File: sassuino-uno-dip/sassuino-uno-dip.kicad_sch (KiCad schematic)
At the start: 30 parts, among them J1 USB_B, J10 OSCPWR_HDR, J2 POWER2_HDR, J3 ICSP_HDR, J4 POWER_HDR, J5 PORTC_HDR, J6 PORTB_HDR, J7 PORTD_HDR, J8 XTAL2_HDR, J9 XTAL1_HDR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

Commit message: Add the actual footprint/model of the pushbutton switch I'm using.
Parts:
- removed SW1: RESET_SW, Button_Switch_THT:SW_PUSH_6mm, symbol Switch:SW_Push
- added SW1: RESET_SW, 0SassuinoFP:SW4_1825910-B_TEC, symbol Switch:SW_Push_Dual
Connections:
- net GND: now also SW1.1, SW1.3
- net ~{RESET}: now also SW1.2, SW1.4
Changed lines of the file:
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@@
   (junction (at 209.55 64.77) (diameter 0) (color 0 0 0 0)
+  )
+  (junction (at 113.03 74.93) (diameter 0) (color 0 0 0 0)
+  )
+  (junction (at 113.03 64.77) (diameter 0) (color 0 0 0 0)
   )
   (junction (at 172.72 38.1) (diameter 0) (color 0 0 0 0)
@@
     (stroke (width 0) (type default) (color 0 0 0 0))
   )
+  (wire (pts (xy 113.03 74.93) (xy 115.57 74.93))
+    (stroke (width 0) (type default) (color 0 0 0 0))
+  )
   (wire (pts (xy 25.4 148.59) (xy 39.37 148.59))
     (stroke (width 0) (type default) (color 0 0 0 0))
@@
     (stroke (width 0) (type default) (color 0 0 0 0))
   )
+  (wire (pts (xy 110.49 64.77) (xy 113.03 64.77))
+    (stroke (width 0) (type default) (color 0 0 0 0))
+  )
   (wire (pts (xy 210.82 100.33) (xy 195.58 100.33))
     (stroke (width 0) (type default) (color 0 0 0 0))
@@
     (stroke (width 0) (type default) (color 0 0 0 0))
   )
+  (wire (pts (xy 110.49 74.93) (xy 113.03 74.93))
+    (stroke (width 0) (type default) (color 0 0 0 0))
+  )
   (wire (pts (xy 58.42 55.88) (xy 60.96 55.88))
     (stroke (width 0) (type default) (color 0 0 0 0))
@@
     (stroke (width 0) (type default) (color 0 0 0 0))
   )
+  (wire (pts (xy 113.03 76.2) (xy 113.03 74.93))
+    (stroke (width 0) (type default) (color 0 0 0 0))
+  )
   (wire (pts (xy 209.55 64.77) (xy 210.82 64.77))
     (stroke (width 0) (type default) (color 0 0 0 0))
@@
     (stroke (width 0) (type default) (color 0 0 0 0))
   )
+  (wire (pts (xy 113.03 64.77) (xy 115.57 64.77))
+    (stroke (width 0) (type default) (color 0 0 0 0))
+  )
   (wire (pts (xy 34.29 153.67) (xy 34.29 156.21))
     (stroke (width 0) (type default) (color 0 0 0 0))
@@
   )
   (wire (pts (xy 58.42 53.34) (xy 60.96 53.34))
+    (stroke (width 0) (type default) (color 0 0 0 0))
+  )
+  (wire (pts (xy 113.03 60.96) (xy 113.03 64.77))
     (stroke (width 0) (type default) (color 0 0 0 0))
   )
@@
     )
     (pin "1")
+  )
+  (symbol (lib_id "Switch:SW_Push_Dual") (at 110.49 69.85 90) (unit 1)
+    (in_bom yes) (on_board yes) (fields_autoplaced)
+    (property "Reference" "SW1" (id 0) (at 116.84 68.5799 90)
+      (effects (font (size 1.27 1.27)) (justify right))
+    )
+    (property "Value" "RESET_SW" (id 1) (at 116.84 71.1199 90)
+      (effects (font (size 1.27 1.27)) (justify right))
+    )
+    (property "Footprint" "0SassuinoFP:SW4_1825910-B_TEC" (id 2) (at 105.41 69.85 0)
+      (effects (font (size 1.27 1.27)) hide)
+    )
+    (property "Datasheet" "https://www.te.com/usa-en/product-1825910-7.datasheet.pdf" (id 3) (at 105.41 69.85 0)
+      (effects (font (size 1.27 1.27)) hide)
+    )
+    (pin "1")
+    (pin "2")
+    (pin "3")
+    (pin "4")
   )
   (symbol (lib_id "Connector_Generic:Conn_01x08") (at 44.45 148.59 0) (unit 1)
@@
     (pin "2")
   )
-  (symbol (lib_id "Switch:SW_Push") (at 113.03 66.04 90) (unit 1)
-    (in_bom yes) (on_board yes) (fields_autoplaced)
-    (property "Reference" "SW1" (id 0) (at 114.3 64.7699 90)
-      (effects (font (size 1.27 1.27)) (justify right))
-    )
-    (property "Value" "RESET_SW" (id 1) (at 114.3 67.3099 90)
-      (effects (font (size 1.27 1.27)) (justify right))
-    )
-    (property "Footprint" "Button_Switch_THT:SW_PUSH_6mm" (id 2) (at 107.95 66.04 0)
-      (effects (font (size 1.27 1.27)) hide)
-    )
-    (property "Datasheet" "~" (id 3) (at 107.95 66.04 0)
-      (effects (font (size 1.27 1.27)) hide)
-    )
-    (pin "1")
-    (pin "2")
-  )
   (symbol (lib_id "power:VCC") (at 102.87 182.88 0) (unit 1)
     (in_bom yes) (on_board yes) (fields_autoplaced)
@@
     (pin "1")
   )
-  (symbol (lib_id "power:GND") (at 113.03 71.12 0) (unit 1)
-    (in_bom yes) (on_board yes) (fields_autoplaced)
-    (property "Reference" "#PWR0111" (id 0) (at 113.03 77.47 0)
-      (effects (font (size 1.27 1.27)) hide)
-    )
-    (property "Value" "GND" (id 1) (at 113.03 76.2 0))
-    (property "Footprint" "" (id 2) (at 113.03 71.12 0)
-      (effects (font (size 1.27 1.27)) hide)
-    )
-    (property "Datasheet" "" (id 3) (at 113.03 71.12 0)
+  (symbol (lib_id "power:GND") (at 113.03 76.2 0) (unit 1)
+    (in_bom yes) (on_board yes) (fields_autoplaced)
+    (property "Reference" "#PWR0111" (id 0) (at 113.03 82.55 0)
+      (effects (font (size 1.27 1.27)) hide)
+    )
+    (property "Value" "GND" (id 1) (at 113.03 81.28 0))
+    (property "Footprint" "" (id 2) (at 113.03 76.2 0)
+      (effects (font (size 1.27 1.27)) hide)
+    )
+    (property "Datasheet" "" (id 3) (at 113.03 76.2 0)
       (effects (font (size 1.27 1.27)) hide)
     )
@@
       (reference "R3") (unit 1) (value "10K") (footprint "Resistor_SMD:R_1206_3216Metric")
     )
-    (path "/75a043c9-9e49-4414-80bf-ac27bb36e4e0"
-      (reference "SW1") (unit 1) (value "RESET_SW") (footprint "Button_Switch_THT:SW_PUSH_6mm")
+    (path "/126610dc-fcb3-4c6a-b444-35d67e624073"
+      (reference "SW1") (unit 1) (value "RESET_SW") (footprint "0SassuinoFP:SW4_1825910-B_TEC")
     )
     (path "/d4ca7310-101e-466b-b5be-c8ae191213f7"

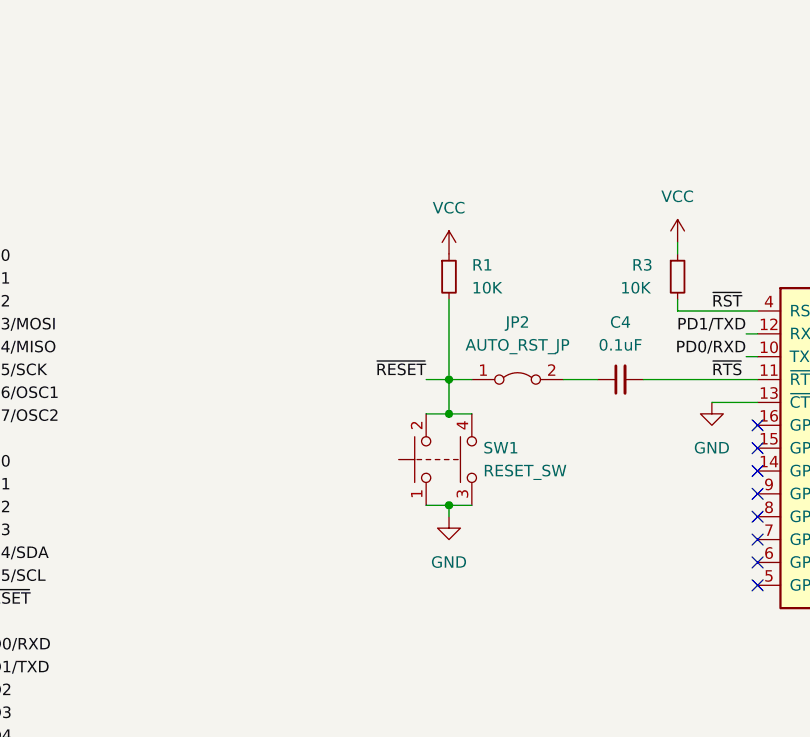
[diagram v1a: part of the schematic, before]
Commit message: Add a clamp diode to the reset circuit.
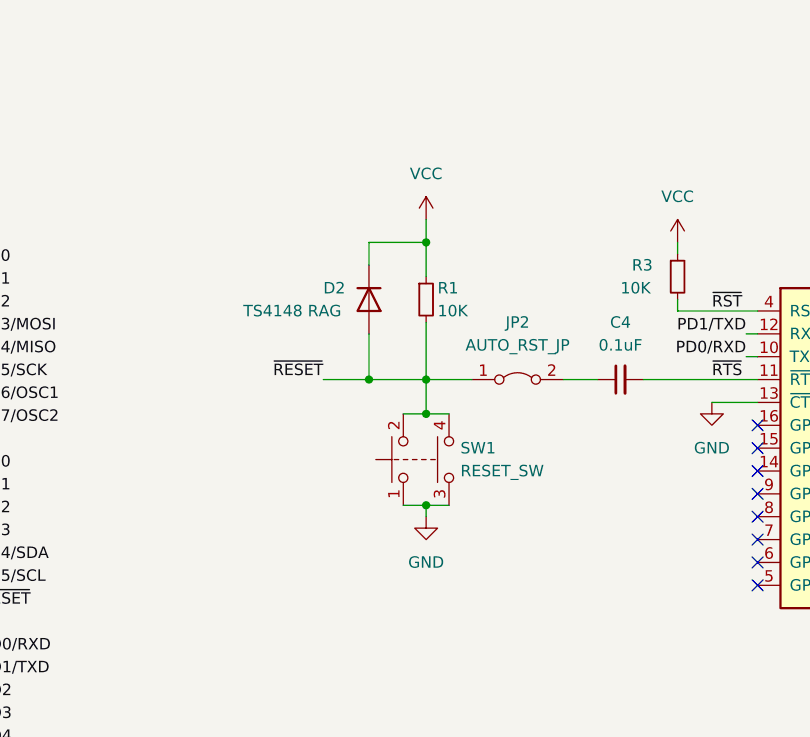
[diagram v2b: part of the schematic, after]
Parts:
- added D2: TS4148 RAG, Diode_SMD:D_1206_3216Metric, symbol Device:D
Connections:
- net VCC: now also D2.1 (K)
- net ~{RESET}: now also D2.2 (A)
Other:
- moved on the sheet: R1, SW1

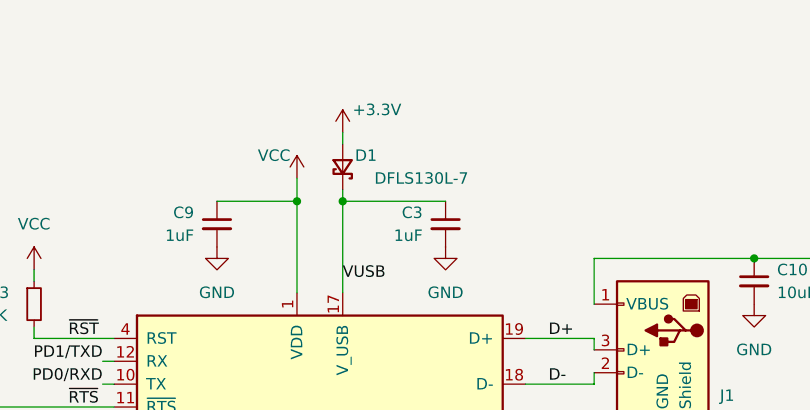
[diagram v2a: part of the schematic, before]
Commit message: Add missing PWR_FLAG so the schematic passes the ERC again.
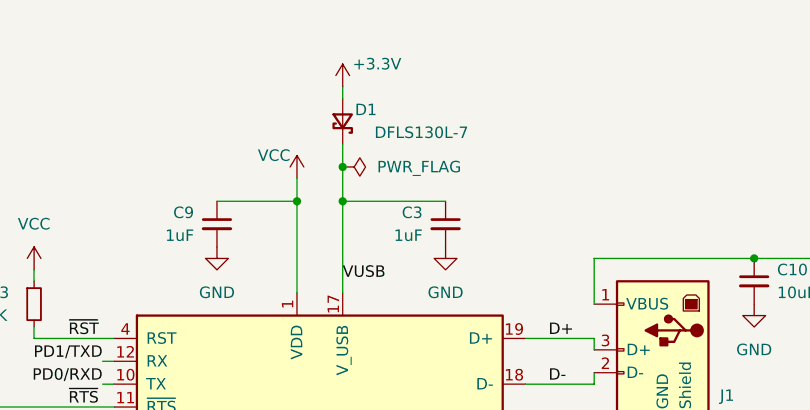
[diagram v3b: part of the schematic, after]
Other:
- moved on the sheet: D1
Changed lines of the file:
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@@
   (junction (at 204.47 138.43) (diameter 0) (color 0 0 0 0)
+  )
+  (junction (at 172.72 34.29) (diameter 0) (color 0 0 0 0)
   )
   (junction (at 110.49 45.72) (diameter 0) (color 0 0 0 0)
@@
     (stroke (width 0) (type default) (color 0 0 0 0))
   )
-  (wire (pts (xy 172.72 36.83) (xy 172.72 38.1))
+  (wire (pts (xy 172.72 31.75) (xy 172.72 34.29))
     (stroke (width 0) (type default) (color 0 0 0 0))
   )
@@
     (stroke (width 0) (type default) (color 0 0 0 0))
   )
-  (wire (pts (xy 172.72 30.48) (xy 172.72 31.75))
+  (wire (pts (xy 172.72 25.4) (xy 172.72 26.67))
     (stroke (width 0) (type default) (color 0 0 0 0))
   )
@@
   )
   (wire (pts (xy 193.04 53.34) (xy 200.66 53.34))
+    (stroke (width 0) (type default) (color 0 0 0 0))
+  )
+  (wire (pts (xy 172.72 34.29) (xy 172.72 38.1))
     (stroke (width 0) (type default) (color 0 0 0 0))
   )
@@
     (pin "1")
   )
+  (symbol (lib_id "power:PWR_FLAG") (at 172.72 34.29 270) (unit 1)
+    (in_bom yes) (on_board yes) (fields_autoplaced)
+    (property "Reference" "#FLG0101" (id 0) (at 174.625 34.29 0)
+      (effects (font (size 1.27 1.27)) hide)
+    )
+    (property "Value" "PWR_FLAG" (id 1) (at 176.53 34.2899 90)
+      (effects (font (size 1.27 1.27)) (justify left))
+    )
+    (property "Footprint" "" (id 2) (at 172.72 34.29 0)
+      (effects (font (size 1.27 1.27)) hide)
+    )
+    (property "Datasheet" "~" (id 3) (at 172.72 34.29 0)
+      (effects (font (size 1.27 1.27)) hide)
+    )
+    (pin "1")
+  )
   (symbol (lib_id "power:VCC") (at 234.95 146.05 0) (unit 1)
     (in_bom yes) (on_board yes) (fields_autoplaced)
@@
     (pin "2")
   )
-  (symbol (lib_id "Device:D_Schottky_Small") (at 172.72 34.29 270) (mirror x) (unit 1)
+  (symbol (lib_id "Device:D_Schottky_Small") (at 172.72 29.21 270) (mirror x) (unit 1)
     (in_bom yes) (on_board yes)
-    (property "Reference" "D1" (id 0) (at 176.53 33.02 90)
+    (property "Reference" "D1" (id 0) (at 176.53 27.94 90)
       (effects (font (size 1.27 1.27)) (justify right))
     )
-    (property "Value" "DFLS130L-7" (id 1) (at 186.69 35.56 90)
+    (property "Value" "DFLS130L-7" (id 1) (at 186.69 30.48 90)
       (effects (font (size 1.27 1.27)) (justify right))
     )
-    (property "Footprint" "Diode_SMD:D_PowerDI-123" (id 2) (at 172.72 34.29 90)
-      (effects (font (size 1.27 1.27)) hide)
-    )
-    (property "Datasheet" "https://www.diodes.com/assets/Datasheets/DFLS130L.pdf" (id 3) (at 172.72 34.29 90)
+    (property "Footprint" "Diode_SMD:D_PowerDI-123" (id 2) (at 172.72 29.21 90)
+      (effects (font (size 1.27 1.27)) hide)
+    )
+    (property "Datasheet" "https://www.diodes.com/assets/Datasheets/DFLS130L.pdf" (id 3) (at 172.72 29.21 90)
       (effects (font (size 1.27 1.27)) hide)
     )
@@
     (pin "1")
   )
-  (symbol (lib_id "power:+3.3V") (at 172.72 30.48 0) (mirror y) (unit 1)
+  (symbol (lib_id "power:+3.3V") (at 172.72 25.4 0) (mirror y) (unit 1)
     (in_bom yes) (on_board yes)
-    (property "Reference" "#PWR02" (id 0) (at 172.72 34.29 0)
-      (effects (font (size 1.27 1.27)) hide)
-    )
-    (property "Value" "+3.3V" (id 1) (at 176.53 27.94 0))
-    (property "Footprint" "" (id 2) (at 172.72 30.48 0)
-      (effects (font (size 1.27 1.27)) hide)
-    )
-    (property "Datasheet" "" (id 3) (at 172.72 30.48 0)
+    (property "Reference" "#PWR02" (id 0) (at 172.72 29.21 0)
+      (effects (font (size 1.27 1.27)) hide)
+    )
+    (property "Value" "+3.3V" (id 1) (at 176.53 22.86 0))
+    (property "Footprint" "" (id 2) (at 172.72 25.4 0)
+      (effects (font (size 1.27 1.27)) hide)
+    )
+    (property "Datasheet" "" (id 3) (at 172.72 25.4 0)
       (effects (font (size 1.27 1.27)) hide)
     )
@@
   )
   (symbol_instances
+    (path "/5363497a-4179-4df5-acfd-489da65e4609"
+      (reference "#FLG0101") (unit 1) (value "PWR_FLAG") (footprint "")
+    )
     (path "/1eb342cb-074c-4750-9652-926960d0a3e3"
       (reference "#FLG0102") (unit 1) (value "PWR_FLAG") (footprint "")

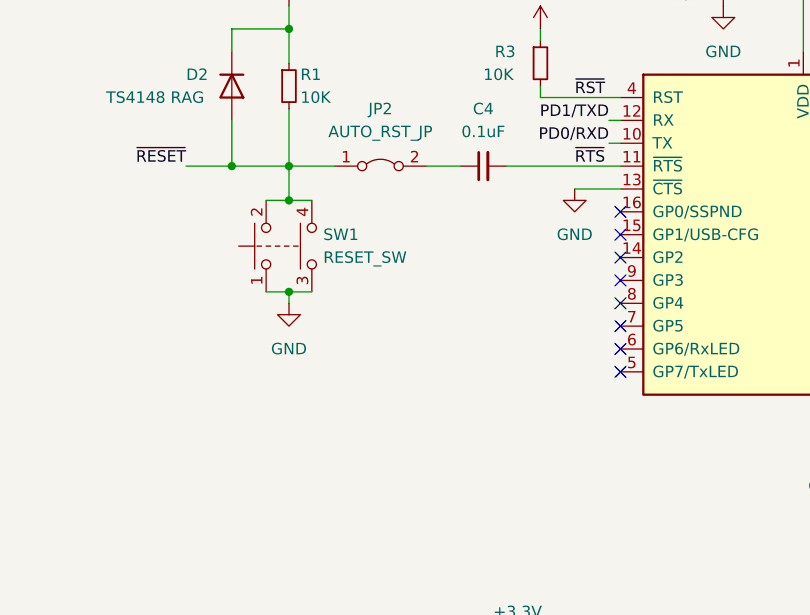
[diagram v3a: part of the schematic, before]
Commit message: Improve the reset circuit.
Add a 330R between the pushbutton reset switch and the capacitor, as
per the AVR hardware design doc.

Pull down the RTS# side of the capacitor with a 1K like in the Arduino
schematic.
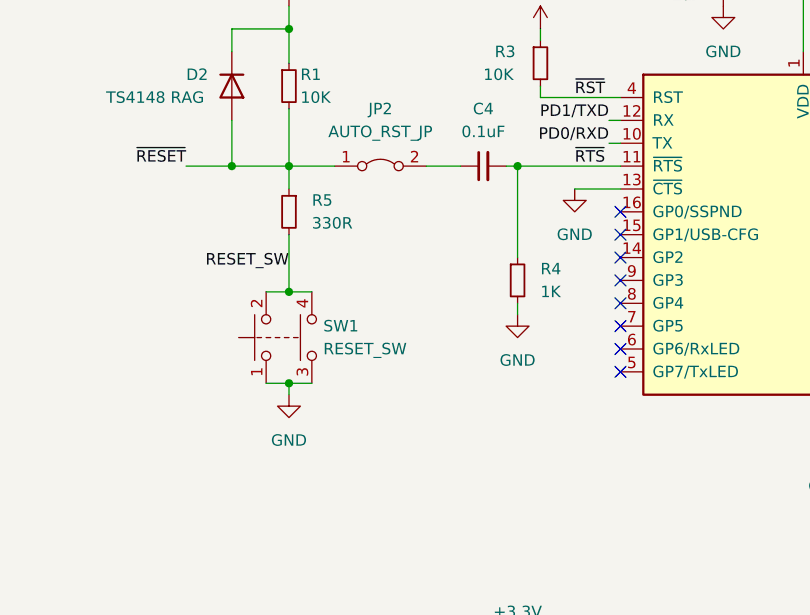
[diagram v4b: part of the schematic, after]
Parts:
- added R4: 1K, Resistor_SMD:R_1206_3216Metric, symbol Device:R_Small
- added R5: 330R, Resistor_SMD:R_1206_3216Metric, symbol Device:R_Small
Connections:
- net GND: now also R4.2
- net ~{RESET}: now also R5.1; no longer SW1.2, SW1.4
- net ~{RTS}: now also R4.1
- new net RESET_SW: R5.2, SW1.2, SW1.4
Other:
- moved on the sheet: SW1

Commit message: Connect the Vin header pin.
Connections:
- net +5V: now also J4.8 (Pin_8)
- no-connect marks 15 -> 14
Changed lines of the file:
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@@
   (junction (at 110.49 74.93) (diameter 0) (color 0 0 0 0)
+  )
+  (junction (at 36.83 151.13) (diameter 0) (color 0 0 0 0)
   )
   (junction (at 135.89 60.96) (diameter 0) (color 0 0 0 0)
@@
   (no_connect (at 218.44 143.51))
   (no_connect (at 238.76 143.51))
-  (no_connect (at 39.37 158.75))
   (no_connect (at 39.37 140.97))
   (no_connect (at 190.5 143.51))
@@
     (stroke (width 0) (type default) (color 0 0 0 0))
   )
+  (wire (pts (xy 39.37 158.75) (xy 36.83 158.75))
+    (stroke (width 0) (type default) (color 0 0 0 0))
+  )
   (wire (pts (xy 85.09 187.96) (xy 87.63 187.96))
     (stroke (width 0) (type default) (color 0 0 0 0))
@@
     (stroke (width 0) (type default) (color 0 0 0 0))
   )
-  (wire (pts (xy 19.05 151.13) (xy 39.37 151.13))
+  (wire (pts (xy 19.05 151.13) (xy 36.83 151.13))
     (stroke (width 0) (type default) (color 0 0 0 0))
   )
@@
     (stroke (width 0) (type default) (color 0 0 0 0))
   )
+  (wire (pts (xy 36.83 151.13) (xy 39.37 151.13))
+    (stroke (width 0) (type default) (color 0 0 0 0))
+  )
   (wire (pts (xy 107.95 85.09) (xy 110.49 85.09))
     (stroke (width 0) (type default) (color 0 0 0 0))
@@
     (stroke (width 0) (type default) (color 0 0 0 0))
   )
+  (wire (pts (xy 36.83 158.75) (xy 36.83 151.13))
+    (stroke (width 0) (type default) (color 0 0 0 0))
+  )

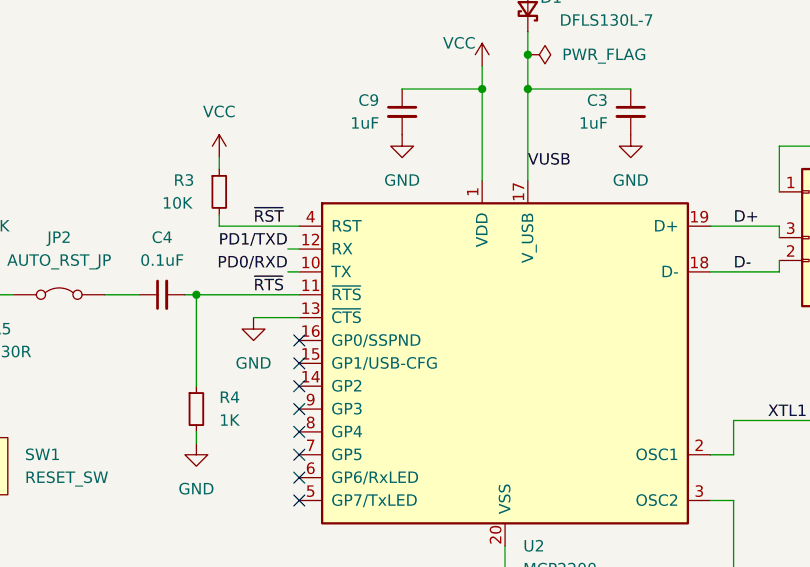
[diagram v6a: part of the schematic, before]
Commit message: Minor tweaks to PCB traces and copper fill zones.
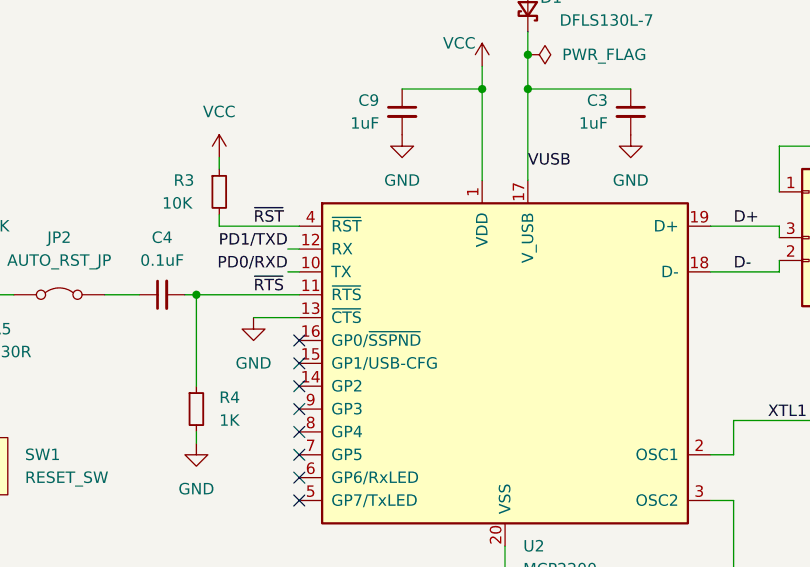
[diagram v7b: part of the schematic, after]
